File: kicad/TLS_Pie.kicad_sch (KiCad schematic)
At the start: 20 parts, among them M1 stepper + 50:1, U1 DS3231 breakout, U10 fan 5 V, U11 INA226 -- NOT FITTED, U12 BCD5A -> 16.8 V / 1.5 A, U3 LM2596S-ADJ -> 5.1 V, U4 Big Easy Driver, U7 VLP-16 interface box, U8 Velodyne VLP-16

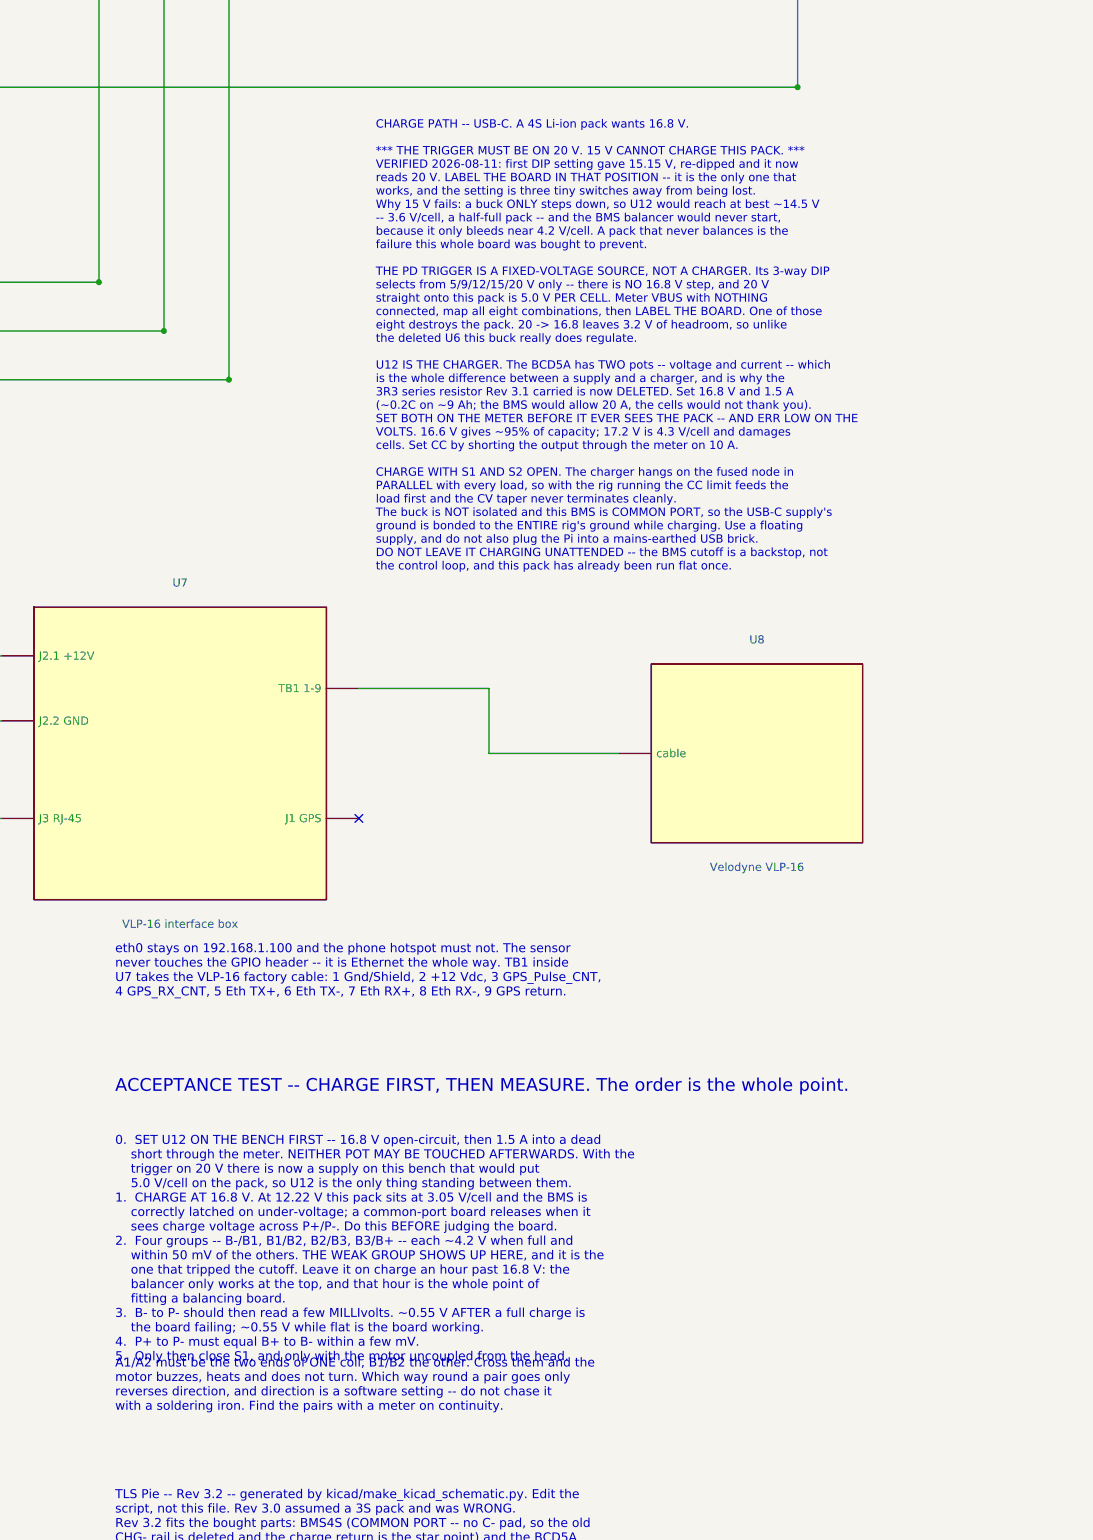
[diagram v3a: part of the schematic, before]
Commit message: Charger set and verified: 16.8 V / 1.5 A -- and why the board looked broken
The BCD5A's pots are multi-turn and ship at MAXIMUM, so a new board reads
20 V in / 20 V out and a few turns of the trimmer changes nothing.  It is not
faulty: the set point starts at 36 V and you have to wind DOWN about forty
turns to come below the input, ideally with a small dummy load, because at
zero load there is no feedback to watch.  The current pot at its
counter-clockwise stop is minimum -- which presents as no current at all.

That cost an evening, so it is now on the sheet, in the restart pointer and in
memory rather than in anyone's head.

Also recorded, because it is the next thing that will look like a fault: the
output reads PACK voltage, not 16.8 V, the moment a flat pack is connected.
That is CC mode holding 1.5 A, and it climbs as the pack fills.  Someone who
does not expect it will reach for the pots and undo the setting.

Meter notes for the EM820DL: the 10 A range needs the red lead in its own
jack, and that jack is unfused -- a bare short, safe across a current-limited
buck and never across the pack.

Verified: 1912 validator checks 0 failed; KiCad ERC 0 violations.

Co-Authored-By: Claude Opus 5 <noreply@anthropic.com>
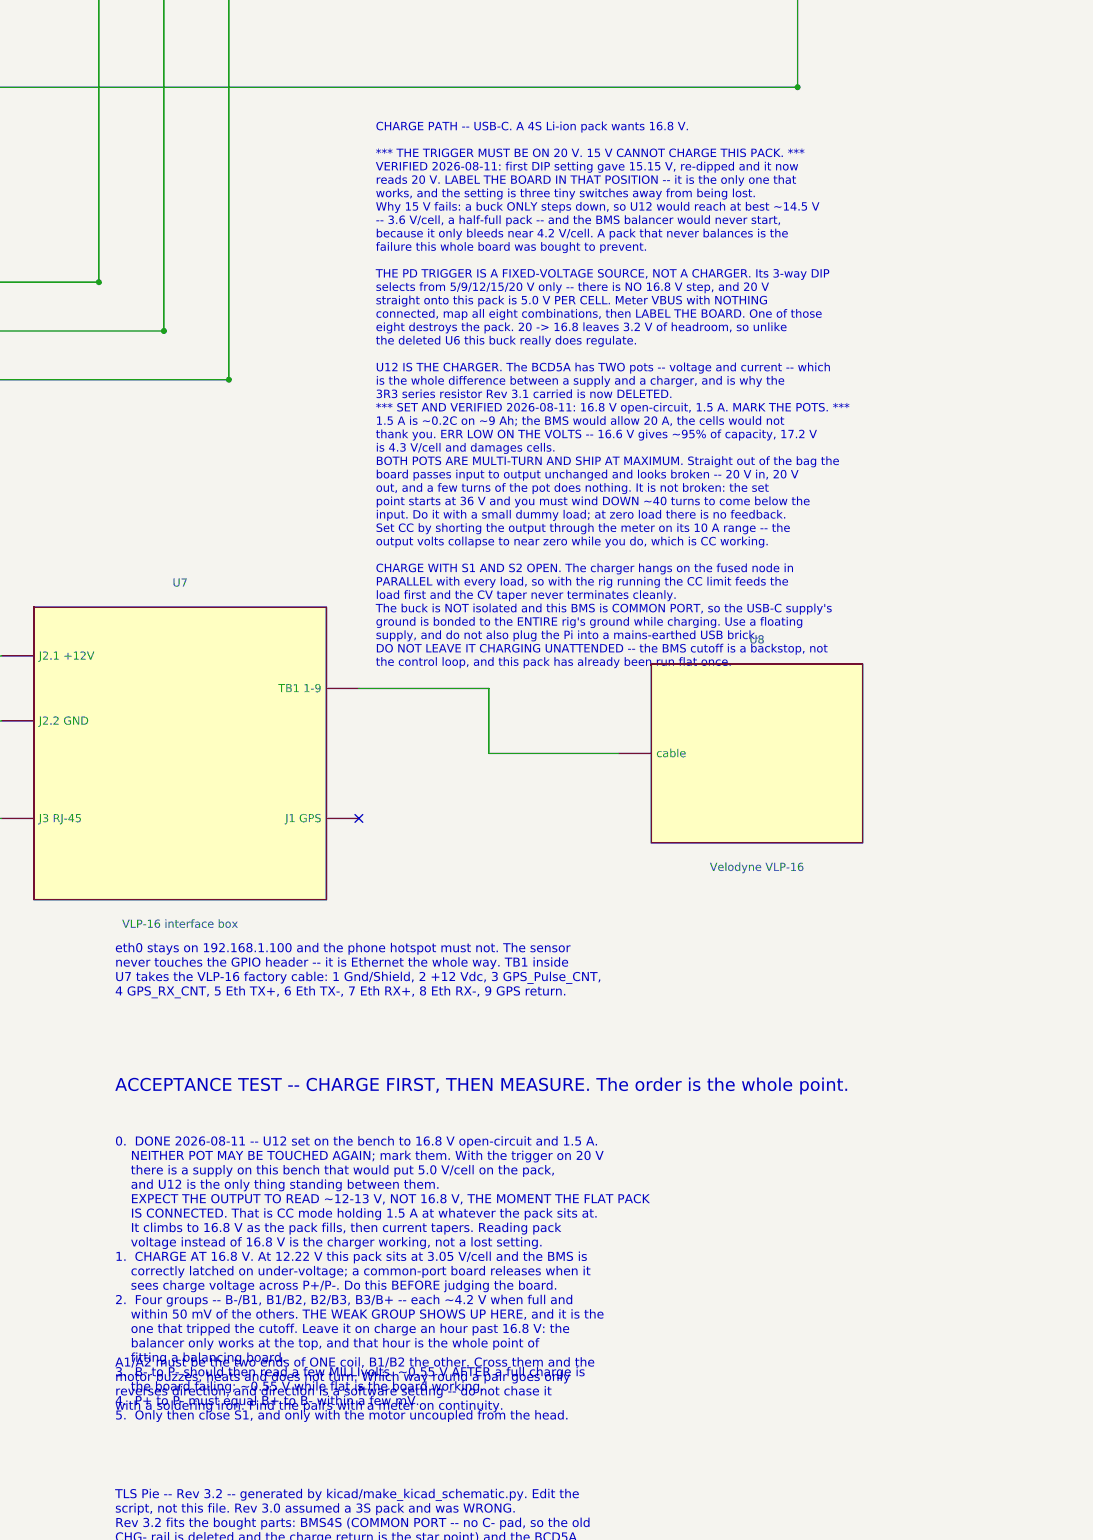
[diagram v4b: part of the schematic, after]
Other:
- note added: "0. DONE 2026-08-11 -- U12 set on the bench to 16.8 V open-circuit and 1.5 A. NEITHER POT MAY BE TOUCHED AGAIN; mark them. With the trigger on 20 V there is a supply on this bench that would put 5.0 V/cell on the pack, and U12 is the only thing standing between them. EXPECT THE OUTPUT TO READ ~12-13 V, NOT 16.8 V, THE MOMENT THE FLAT PACK IS CONNECTED. That is CC mode holding 1.5 A at whatever the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"
- note removed: "0. SET U12 ON THE BENCH FIRST -- 16.8 V open-circuit, then 1.5 A into a dead short through the meter. NEITHER POT MAY BE TOUCHED AFTERWARDS. With the trigger on 20 V there is now a supply on this bench that would put 5.0 V/cell on the pack, so U12 is the only thing standing between them. 1. CHARGE AT 16.8 V. At 12.22 V this pack sits at 3.05 V/cell and the BMS is correctly latched on under-voltag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"

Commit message: Pads verified against the board: this BMS names its taps by voltage
The one assumption Rev 3.2 flagged as unverified is now settled by a photo of
the board itself.  It does not label its taps B1/B2/B3 -- it labels them by
voltage, 0V / 4.2V / 8.4V / 12.6V / 16.8V, and its two output pads carry a
circled minus and plus rather than P- and P+.  The sheet now shows what is
actually printed, because the silkscreen is what you read with a wire in your
hand.

Seven pads, five taps and two outputs, confirms common port with no C-.

Two things worth having in writing, both of which will otherwise read as
faults:

  * those voltages are FULL-CHARGE values.  Metering the taps on a flat pack
    gives roughly 0 / 3.06 / 6.12 / 9.18 / 12.24 V, and what matters is the
    order and the even spacing, not the numbers matching the labels.
  * this board's under-voltage floor is 2.5 V/cell = 10.0 V, so at the
    measured 12.24 V it is NOT latched and P+/P- already carries full pack
    voltage.  The ~0.55 V body-diode reading that started this entire
    investigation belonged to the OLD board's higher threshold, and expecting
    it here would be reading last month's board.

Verified: 1912 validator checks 0 failed; KiCad ERC 0 violations.

Co-Authored-By: Claude Opus 5 <noreply@anthropic.com>
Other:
- note added: "CONNECT THE TAPS IN THIS ORDER: 0V 4.2V 8.4V 12.6V 16.8V The board names its pads by voltage, and those are FULL-CHARGE values -- NOT what a flat pack measures. Against 0V at the measured 12.24 V total you should read roughly: 0 / 3.06 / 6.12 / 9.18 / 12.24 V. WHAT MATTERS IS THE ORDER, evenly spaced and ascending. Meter every tap on the free connector BEFORE plugging it in. The protection ICs ar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"
- note removed: "CONNECT THE TAPS IN THIS ORDER: B- B1 B2 B3 B+ Measured against B-, they are the voltage ladder the vendor specifies: B- = 0 V B1 = 4.2 V B2 = 8.4 V B3 = 12.6 V B+ = 16.8 V METER EACH ONE ON THE FREE CONNECTOR BEFORE PLUGGING IT IN. On a flat pack they read low and evenly spaced -- what matters is the ORDER and that no two are swapped. The protection ICs are powered from the taps. Out of order, o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"

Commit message: Add the panel meter -- and it splits the ground, so draw it that way
The Cricklewood DPM's thick pair IS its shunt, and on this class of meter the
shunt is in the NEGATIVE leg.  So it goes in the return, between the rig's
ground and P- -- not in the +VBATT rail where U11 goes.  GND and P- are now
two nets joined ONLY through PM1, and they cross twice on the sheet with no
junction dot.  Bridge them anywhere and the shunt is shorted out: the meter
reads 0.00 A for ever and nothing warns you, which is why there is now an
assertion for exactly that.

Supply comes from +VSW1, never +VBATT.  These meters draw ~20 mA
continuously; on the always-live rail that is ~0.5 Ah/day and would flatten
this ~9 Ah pack in about three weeks of standing -- which is how it got flat
the first time.  On +VSW1 it dies with S1, and VSENSE still reads true pack
volts by tapping +VBATT upstream of the switch.

The charge return sits on the pack side of the shunt, so charging never
pushes current backwards through the meter and PM1 always shows true rig
draw.  It reads 0.00 A while charging, correctly.

The shunt leg is the one unverified assumption and is flagged in three places
with the test that settles it: thin-black to thick-black near zero means
negative leg and this drawing is right.

Both checkers earned their keep here, failing differently.  The validator
caught two drops sharing a via_x -- collinear segments merged into one wire
and shorted the shunt -- plus a rail extended so it ran THROUGH a PWR_FLAG
pin.  KiCad's ERC caught what the validator could not: with a passive shunt
in the return, the rig-side ground had no power-output pin left anywhere on
it.  JP1 pin 6 not driven.

Verified: 2089 validator checks 0 failed; ERC 0 violations; netlist confirms
GND and P- as separate nets bridged only by PM1.

Co-Authored-By: Claude Opus 5 <noreply@anthropic.com>
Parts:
- added PM1: panel meter V+A, symbol TLS_Pie:PanelMeter_VA
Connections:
- net +VBATT: now also PM1.5 (VSENSE)
- net +VSW1: now also PM1.3 (SUP+)
- net GND: now also PM1.1 (I in); no longer BMS1.7 (P-), J_USB.2, U12.2 (OUT-), U12.3 (IN-)
- new net P-: BMS1.7 (P-), J_USB.2, PM1.2 (I out), PM1.4 (SUP-), U12.2 (OUT-), U12.3 (IN-)
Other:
- note added: "PANEL METER PM1 -- and it changes the ground topology, so read this. ITS THICK PAIR IS THE SHUNT, AND THE SHUNT IS IN THE NEGATIVE LEG. So it goes in the RETURN, between the rig's ground and P- -- NOT in the +VBATT rail where U11 goes. GND and P- are now separate nodes joined ONLY through PM1. They cross twice on this sheet with no junction dot and are NOT connected there. Bridge them anywhere an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"
